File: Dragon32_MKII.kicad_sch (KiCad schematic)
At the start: 219 parts, among them IC1 4116, IC10 SFC2318, IC11 4053, IC12 6847, IC13 74LS273, IC14 74LS86, IC15 74LS783, IC16 74LS244, IC17 ROM8K, IC18 ROM8K, IC19 6809E, IC2 4116, IC20 4529, IC21 74LS123, IC22 74LS00, IC23 74LS74, IC24 74LS244, IC25 LM393, IC26 6821, IC27 74LS20, IC28 74LS393, IC29 74LS393, IC3 4116, IC30 74LS32, IC31 74LS02, IC32 74LS390, IC33 74LS138, IC34 4050, IC35 6821, IC36 4116, IC37 4116, IC38 4116, IC39 4116, IC4 4116, IC40 4116, IC41 4116, IC42 4116, IC43 4116, IC5 4116, IC6 4116, IC7 4116, IC8 4116, IC9 LM1889, SW1 RESET, U1 LINE_PULSE_DIAGRAM

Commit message: Moved C52, C54 & C56 from -5V to +12V Fixed some ERC issues
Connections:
- net +12V: now also C52.1, C54.1, C56.1; no longer IC25.8 (V+)
- net -5V: no longer C52.1, C54.1, C56.1
- net GND: no longer IC25.4 (V-)
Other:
- moved on the sheet: C34, C51, C52, C53, C54, C55, C56, R44

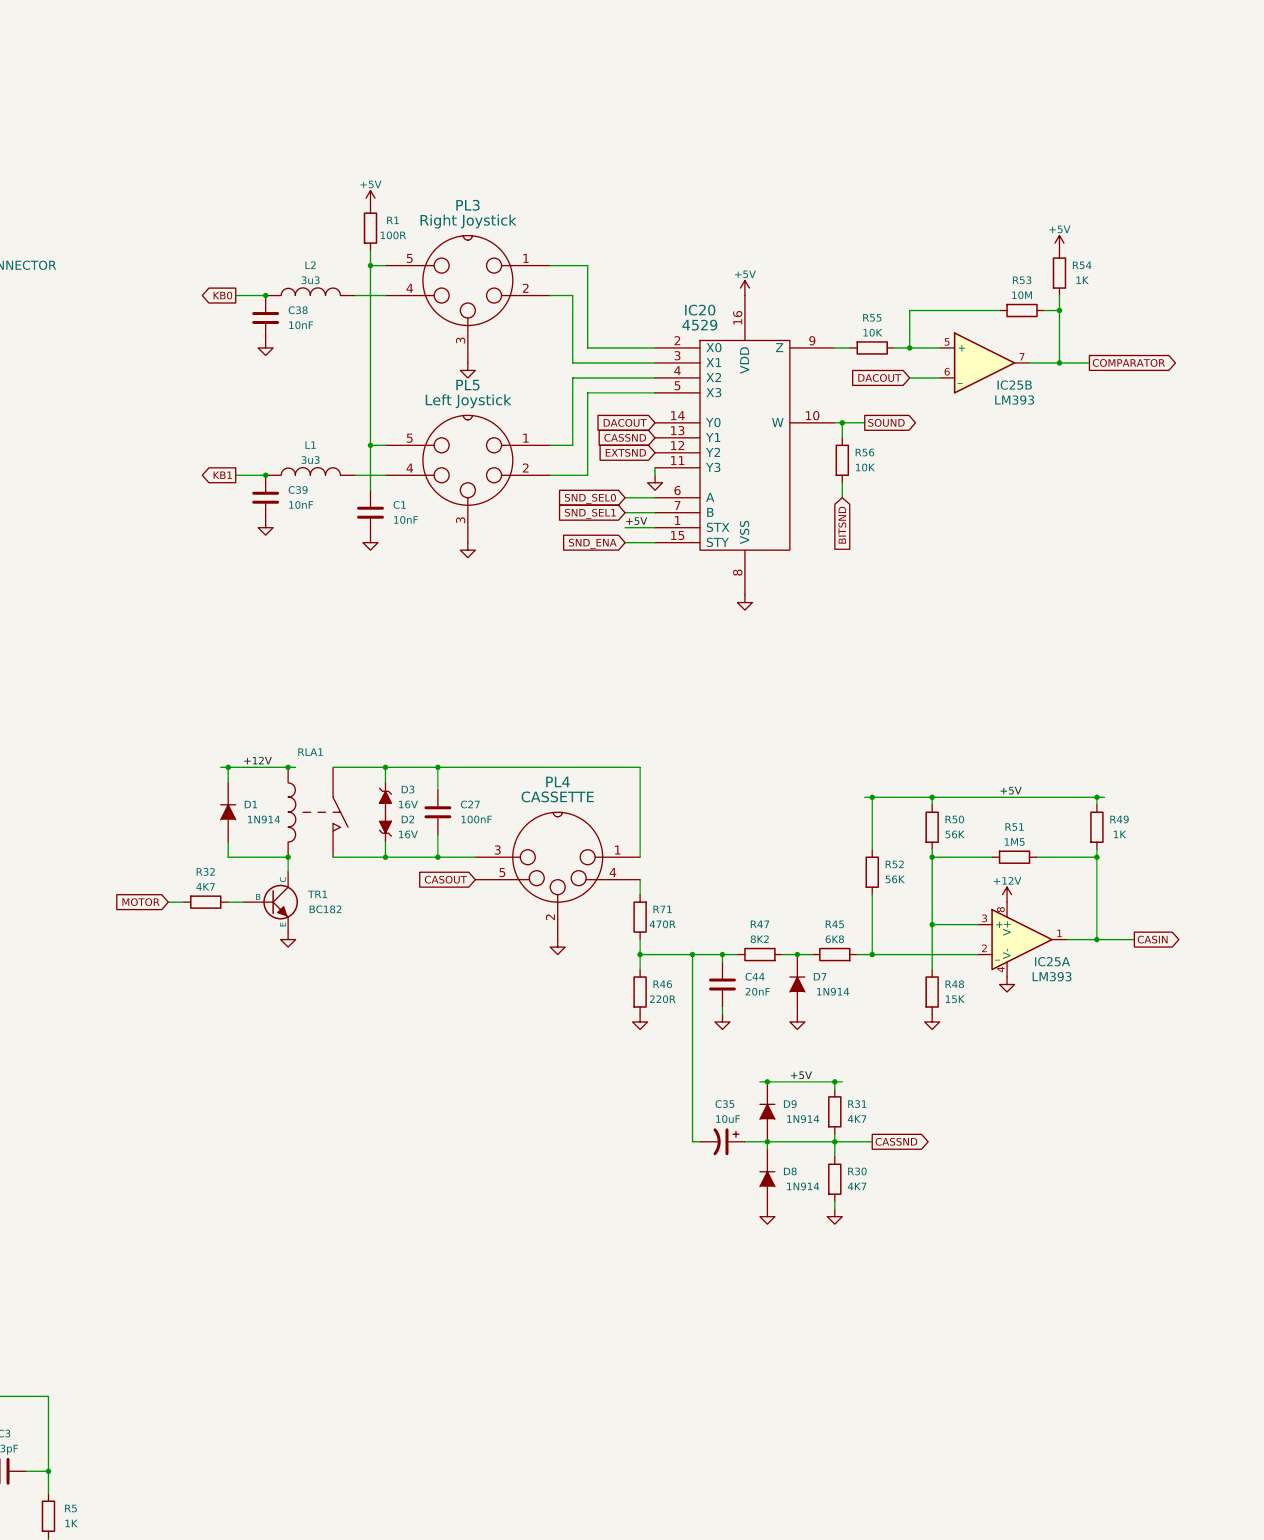
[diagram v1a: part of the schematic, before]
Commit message: Added keyboard matrix info Updated pdf plot
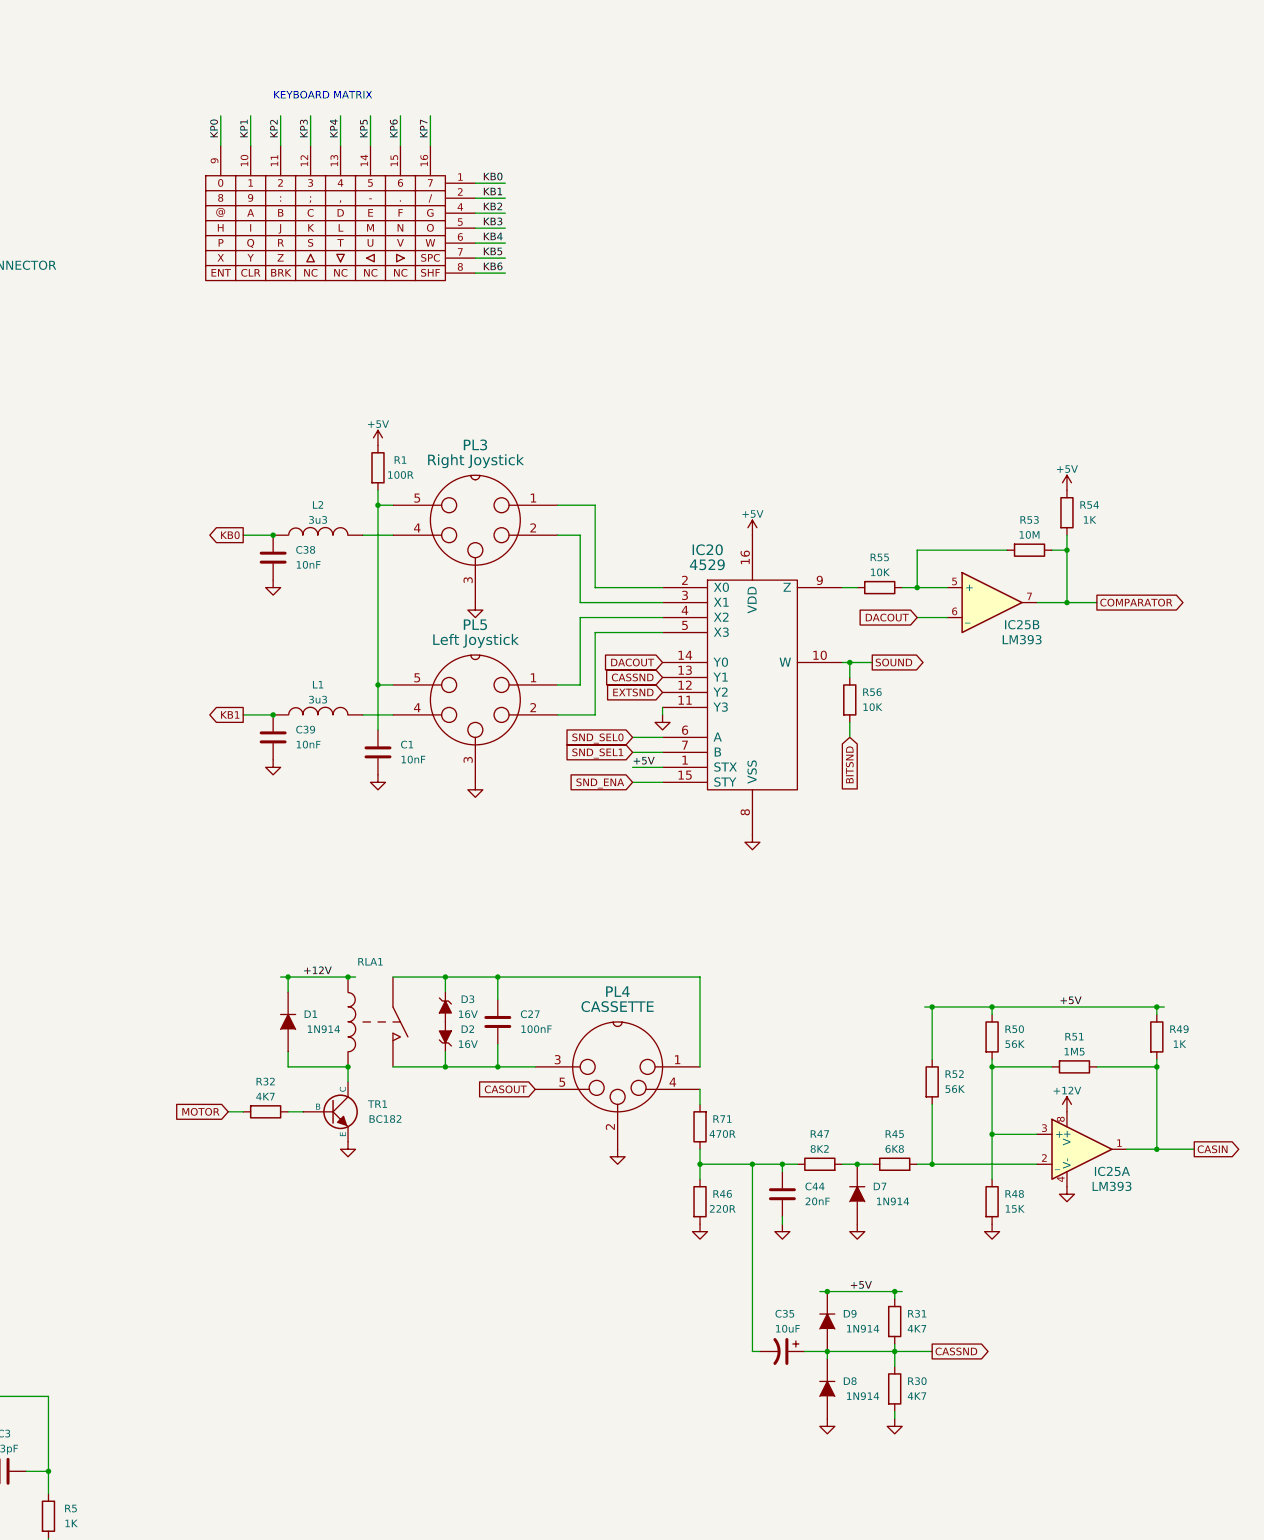
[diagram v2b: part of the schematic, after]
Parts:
- added U2: ~, symbol Dragon32_MKII:DragonKeyboardMatrix
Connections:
- net KB0: now also U2.1
- net KB1: now also U2.2
- net KB2: now also U2.4
- net KB3: now also U2.5
- net KB4: now also U2.6
- net KB5: now also U2.7
- net KB6: now also U2.8
- net KP0: now also U2.9
- net KP1: now also U2.10
- net KP2: now also U2.11
- net KP3: now also U2.12
- net KP4: now also U2.13
- net KP5: now also U2.14
- net KP6: now also U2.15
- net KP7: now also U2.16
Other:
- note added: "KEYBOARD MATRIX"
- moved on the sheet: C1, C27, C35, C38, C39, C44, D1, D2, D3, D7, D8, D9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
